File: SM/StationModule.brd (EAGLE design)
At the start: 62.2 x 36.8 mm, 25 parts, among them IC1 REG1117

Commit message: silkscreen
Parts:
- added D2: PMLL4150, diode:SOD80C
- added R5: 10k, rcl:R0805
- added R6: 33k, rcl:R0805
- added STOP: (no value), pinhead+:1X02
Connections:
- new net ADC: D2.A, R5.2, R6.1, U1.ADC
- new net STOP: R6.2, STOP.2
- net +3V3: now also STOP.1
- net GND: now also D2.C, R5.1; no longer U1.ADC
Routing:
- net ADC: track 0.00 -> 40.4 mm, vias 0 -> 2
- net +3V3: track 97.6 -> 119.7 mm
- net RESET: track 43.9 -> 54.1 mm
- net STOP: track 0.00 -> 2.86 mm
- net GND: track 226.1 -> 228.3 mm, vias 27 -> 22

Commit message: Schematic annotation
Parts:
- moved D2 2.00 mm to (27.5, 50.2), turned to 135 degrees
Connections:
- net ADC: no longer D2.A
- net GND: now also D2.A; no longer D2.C
- net STOP: now also D2.C
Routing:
- net STOP: track 2.86 -> 8.36 mm
- net ADC: track 40.4 -> 37.3 mm
- net GPIO2: track 55.8 -> 56.6 mm
- net GND: track 228.3 -> 228.6 mm, vias 22 -> 23
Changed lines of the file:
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@@
 <layer number="23" name="tOrigins" color="15" fill="1" visible="yes" active="yes"/>
 <layer number="24" name="bOrigins" color="15" fill="1" visible="yes" active="yes"/>
-<layer number="25" name="tNames" color="7" fill="1" visible="yes" active="yes"/>
-<layer number="26" name="bNames" color="7" fill="1" visible="no" active="yes"/>
+<layer number="25" name="tNames" color="7" fill="1" visible="no" active="yes"/>
+<layer number="26" name="bNames" color="7" fill="1" visible="yes" active="yes"/>
 <layer number="27" name="tValues" color="7" fill="1" visible="yes" active="yes"/>
 <layer number="28" name="bValues" color="7" fill="1" visible="no" active="yes"/>
@@
 <wire x1="81.28" y1="81.28" x2="19.05" y2="81.28" width="0" layer="20"/>
 <wire x1="19.05" y1="81.28" x2="19.05" y2="44.45" width="0" layer="20"/>
-<text x="31.75" y="34.29" size="0.762" layer="21">Portland State University
+<text x="34.29" y="38.1" size="0.762" layer="21">Portland State University
 T.Gilbert - 2107</text>
 <text x="75.184" y="71.628" size="1.27" layer="25">5V</text>
@@
 <attribute name="VALUE" x="37.465" y="49.53" size="1.27" layer="27" rot="R180"/>
 </element>
-<element name="D2" library="diode" package="SOD80C" value="PMLL4150" x="29.464" y="50.292" smashed="yes">
-<attribute name="NAME" x="27.94" y="51.435" size="1.016" layer="25"/>
+<element name="D2" library="diode" package="SOD80C" value="PMLL4150" x="27.4628125" y="50.217603125" smashed="yes" rot="R135">
+<attribute name="NAME" x="27.732221875" y="48.33175" size="1.016" layer="25" rot="R135"/>
 </element>
 </elements>
@@
 <wire x1="36.068" y1="51.054" x2="37.592" y2="49.53" width="0.6096" layer="1"/>
 <wire x1="37.592" y1="49.53" x2="43.18" y2="49.53" width="0.6096" layer="1"/>
-<contactref element="D2" pad="C"/>
-<wire x1="27.764" y1="50.292" x2="27.764" y2="51.894" width="0.6096" layer="1"/>
-<wire x1="27.764" y1="51.894" x2="27.94" y2="52.07" width="0.6096" layer="1"/>
-<wire x1="27.94" y1="52.07" x2="33.97" y2="52.07" width="0.6096" layer="1"/>
-<wire x1="33.97" y1="52.07" x2="34.29" y2="51.75" width="0.6096" layer="1"/>
 <wire x1="34.29" y1="51.75" x2="34.29" y2="53.34" width="0.6096" layer="1"/>
 <wire x1="34.29" y1="53.34" x2="36.068" y2="53.34" width="0.6096" layer="1"/>
+<contactref element="D2" pad="A"/>
+<wire x1="26.260728125" y1="51.419684375" x2="26.8804125" y2="50.8" width="0.4064" layer="1"/>
+<wire x1="26.8804125" y1="50.8" x2="31.75" y2="50.8" width="0.4064" layer="1"/>
+<wire x1="31.75" y1="50.8" x2="32.7" y2="51.75" width="0.4064" layer="1"/>
+<wire x1="32.7" y1="51.75" x2="34.29" y2="51.75" width="0.4064" layer="1"/>
+<via x="52.07" y="76.962" extent="1-16" drill="0.6"/>
 </signal>
 <signal name="GPIO1">
@@
 <via x="73.025" y="57.785" extent="1-16" drill="0.6" shape="square"/>
 <wire x1="73.025" y1="57.785" x2="71.18" y2="57.785" width="0.6096" layer="1"/>
-<wire x1="47.244" y1="70.866" x2="35.052" y2="70.866" width="0.6096" layer="16"/>
+<wire x1="54.102" y1="70.866" x2="35.052" y2="70.866" width="0.6096" layer="16"/>
 <via x="35.052" y="70.866" extent="1-16" drill="0.6" shape="square"/>
 <wire x1="35.052" y1="70.866" x2="34.925" y2="70.739" width="0.6096" layer="1"/>
 <wire x1="34.925" y1="70.739" x2="34.925" y2="68.26" width="0.6096" layer="1"/>
-<wire x1="47.244" y1="70.866" x2="48.26" y2="69.85" width="0.6096" layer="16"/>
-<wire x1="48.26" y1="69.85" x2="48.26" y2="62.738" width="0.6096" layer="16"/>
-<wire x1="48.26" y1="62.738" x2="48.768" y2="62.23" width="0.6096" layer="16"/>
 <wire x1="64.77" y1="62.23" x2="55.88" y2="62.23" width="0.6096" layer="16"/>
-<wire x1="54.61" y1="62.23" x2="48.768" y2="62.23" width="0.6096" layer="16"/>
 <wire x1="60.17" y1="61.84" x2="59.78" y2="62.23" width="0.6096" layer="1"/>
 <wire x1="59.78" y1="62.23" x2="55.88" y2="62.23" width="0.6096" layer="1"/>
 <via x="55.88" y="62.23" extent="1-16" drill="0.6" shape="square"/>
-<wire x1="55.88" y1="62.23" x2="54.61" y2="62.23" width="0.6096" layer="16"/>
+<wire x1="54.102" y1="70.866" x2="54.356" y2="70.612" width="0.6096" layer="16"/>
+<wire x1="54.356" y1="70.612" x2="54.356" y2="62.23" width="0.6096" layer="16"/>
+<wire x1="54.356" y1="62.23" x2="55.88" y2="62.23" width="0.6096" layer="16"/>
 </signal>
 <signal name="GPIO0">
@@
 <contactref element="R6" pad="2"/>
 <wire x1="35.88" y1="46.99" x2="33.02" y2="46.99" width="0.6096" layer="1"/>
+<contactref element="D2" pad="C"/>
+<wire x1="28.66489375" y1="49.01551875" x2="28.671375" y2="49.022" width="0.4064" layer="1"/>
+<wire x1="28.671375" y1="49.022" x2="31.496" y2="49.022" width="0.4064" layer="1"/>
+<wire x1="31.496" y1="49.022" x2="33.02" y2="47.498" width="0.4064" layer="1"/>
+<wire x1="33.02" y1="47.498" x2="33.02" y2="46.99" width="0.4064" layer="1"/>
 </signal>
 <signal name="ADC">
@@
 <contactref element="R5" pad="2"/>
 <contactref element="U1" pad="ADC"/>
-<contactref element="D2" pad="A"/>
 <wire x1="43.77" y1="69.84" x2="45.73" y2="69.84" width="0.6096" layer="1"/>
 <wire x1="45.73" y1="69.84" x2="46.482" y2="69.088" width="0.6096" layer="1"/>
 <via x="46.482" y="69.088" extent="1-16" drill="0.6" shape="square"/>
-<wire x1="46.482" y1="69.088" x2="46.482" y2="61.722" width="0.6096" layer="16"/>
-<wire x1="46.482" y1="61.722" x2="41.91" y2="57.15" width="0.6096" layer="16"/>
-<wire x1="41.91" y1="57.15" x2="41.91" y2="48.768" width="0.6096" layer="16"/>
+<wire x1="41.91" y1="58.42" x2="41.91" y2="48.768" width="0.6096" layer="16"/>
 <wire x1="41.91" y1="48.768" x2="41.148" y2="48.006" width="0.6096" layer="16"/>
 <via x="41.148" y="48.006" extent="1-16" drill="0.6" shape="square"/>
@@
 <wire x1="39.37" y1="46.99" x2="40.132" y2="46.99" width="0.6096" layer="1"/>
 <wire x1="40.132" y1="46.99" x2="41.148" y2="48.006" width="0.6096" layer="1"/>
-<wire x1="31.164" y1="50.292" x2="32.258" y2="50.292" width="0.6096" layer="1"/>
-<wire x1="32.258" y1="50.292" x2="33.02" y2="49.53" width="0.6096" layer="1"/>
-<wire x1="33.02" y1="49.53" x2="33.97" y2="49.53" width="0.6096" layer="1"/>
 <wire x1="33.97" y1="49.53" x2="34.29" y2="49.85" width="0.6096" layer="1"/>
 <wire x1="34.29" y1="49.85" x2="35.748" y2="49.85" width="0.6096" layer="1"/>
@@
 <wire x1="39.116" y1="48.006" x2="39.116" y2="47.244" width="0.6096" layer="1"/>
 <wire x1="39.116" y1="47.244" x2="39.37" y2="46.99" width="0.6096" layer="1"/>
-</signal>
-<signal name="N$1">
-<via x="52.07" y="76.962" extent="1-16" drill="0.6"/>
+<wire x1="46.482" y1="69.088" x2="45.72" y2="68.326" width="0.6096" layer="16"/>
+<wire x1="45.72" y1="68.326" x2="45.72" y2="62.23" width="0.6096" layer="16"/>
+<wire x1="45.72" y1="62.23" x2="41.91" y2="58.42" width="0.6096" layer="16"/>
 </signal>
 </signals>
+<errors>
+</errors>
 </board>
 </drawing>

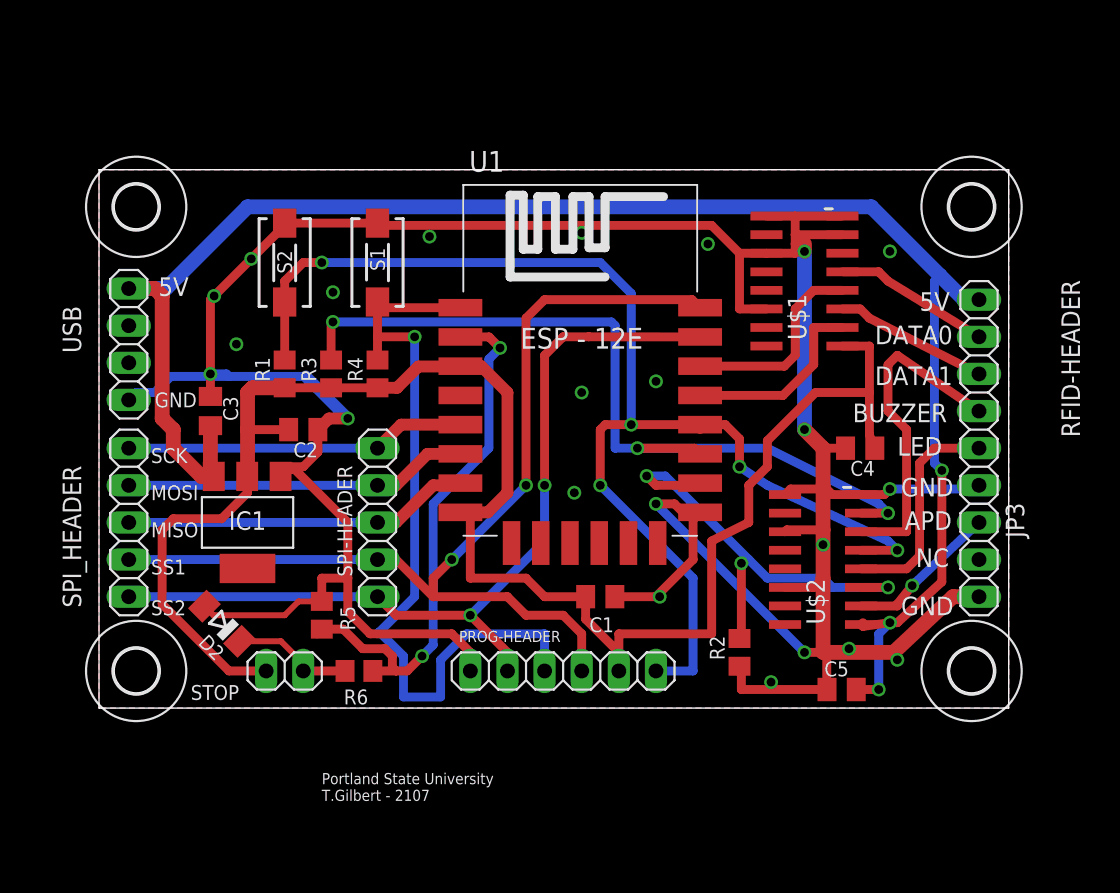
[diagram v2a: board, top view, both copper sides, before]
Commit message: SM v1.1
with fixes
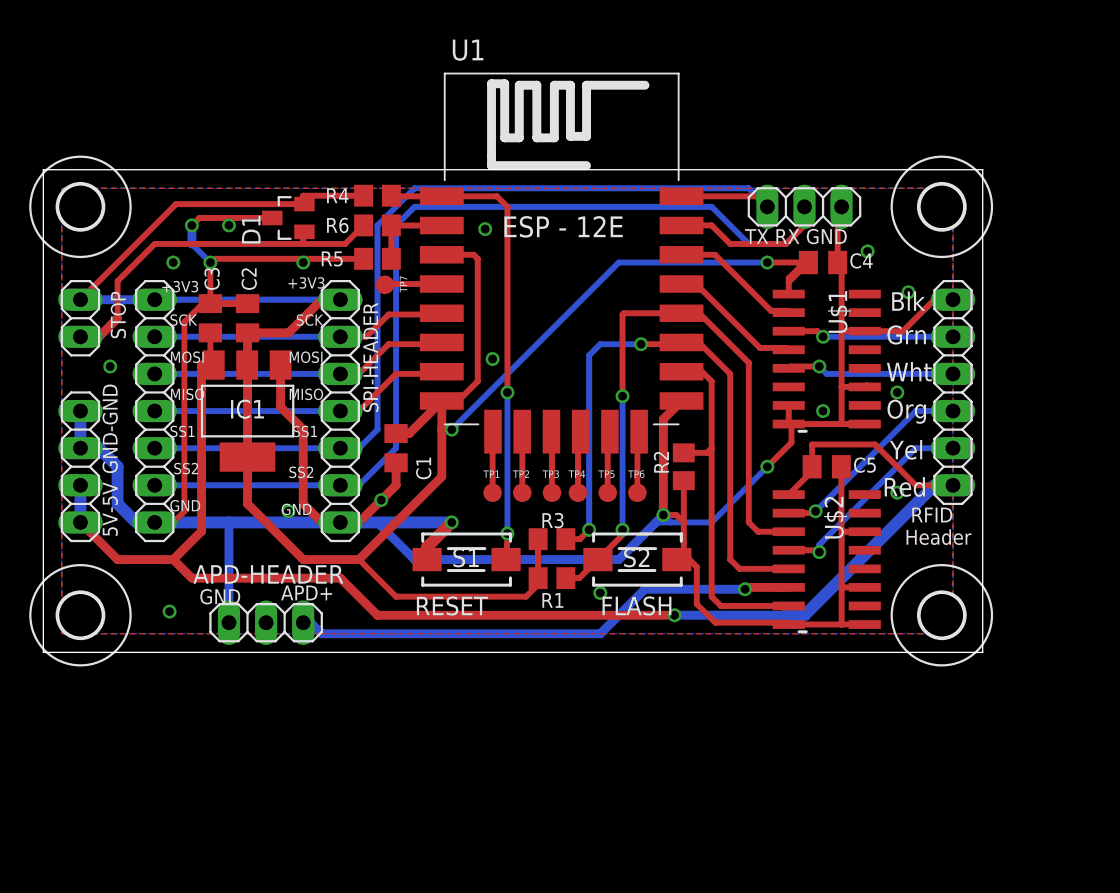
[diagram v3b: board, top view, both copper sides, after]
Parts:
- removed D2: PMLL4150, diode:SOD80C
- removed PROG-HEADER: PROG-HEADER, pinhead+:1X06
- removed SPI_HEADER: SPI-HEADER, pinhead+:1X05
- added D1: MMBZ5V6ALT1G, diode:SOT23
- added JP1: (no value), pinhead+:1X03
- added JP4: (no value), pinhead+:1X07
- added TP1, TP2, TP3, TP4, TP5, TP6, TP7: TPB1,27, testpad:B1,27
- S1: value DTSM-3 -> RESET
- S2: value DTSM-3 -> BOOT-LOADER
- SPI-HEADER: value SPI_HEADER -> (none); device pinhead+:1X05 -> pinhead+:1X07
- USB: value USB-HEADER -> 5V-Power
- moved JP3 49.0 mm to (30.5, 50.3), turned to 180 degrees
- moved S2 31.5 mm to (55.9, 54.6), turned to 0 degrees
- moved R6 30.5 mm to (38.1, 77.5)
- moved STOP 27.9 mm to (17.8, 71.1), turned to 270 degrees
- moved R5 24.7 mm to (38.1, 75.2), turned to 0 degrees
- moved R1 23.0 mm to (50.0, 53.3), turned to 180 degrees
- moved S1 21.2 mm to (44.2, 54.6), turned to 0 degrees
- moved R3 18.9 mm to (50.0, 56.0), turned to 180 degrees
- moved C1 17.3 mm to (39.4, 62.2), turned to 270 degrees
- moved C5 15.3 mm to (68.8, 61.0), turned to 0 degrees
- moved R2 13.3 mm to (59.1, 61.0)
- moved C4 13.0 mm to (68.6, 74.9), turned to 0 degrees
- moved R4 12.2 mm to (38.1, 79.5), turned to 180 degrees
- moved USB 9.01 mm to (17.8, 61.0), turned to 90 degrees
- moved C2 8.52 mm to (29.2, 71.1), turned to 270 degrees
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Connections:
- removed net D+: USB.2
- removed net D-: USB.3
- new net N$1: U$2.10
- new net N$10: TP2.TP, U1.MISO
- new net N$11: TP3.TP, U1.GPIO9
- new net N$12: TP4.TP, U1.GPIO10
- new net N$13: TP5.TP, U1.MOSI
- new net N$15: TP6.TP, U1.SCLK
- new net N$2: U$2.12
- new net N$3: U$2.15
- new net N$4: U$1.6
- new net N$5: U$1.10
- new net N$6: U$1.12
- new net N$7: U$1.15
- new net N$8: TP7.TP, U1.GPIO16
- new net N$9: TP1.TP, U1.CS0
- net +3V3: now also D1.2, IC1.4, JP4.7, SPI-HEADER.1; no longer PROG-HEADER.2
- net +5V: now also RFID-HEADER.6, USB.2; no longer RFID-HEADER.1
- net APD_EN: now also U$2.6; no longer U$2.2
- net BUZZER: now also RFID-HEADER.5, U$2.4; no longer RFID-HEADER.4, U$2.6
- net GND: now also D1.3, JP1.3, JP4.1, RFID-HEADER.1, SPI-HEADER.7, USB.3; no longer D2.A, PROG-HEADER.6, RFID-HEADER.6
- net GPIO0: now also U$2.3; no longer PROG-HEADER.1, U$2.5
- net GPIO1: now also JP1.1, JP4.3, SPI-HEADER.5; no longer PROG-HEADER.3, SPI-HEADER.4, SPI_HEADER.4
- net GPIO12: now also JP4.5, SPI-HEADER.3; no longer SPI-HEADER.2, SPI_HEADER.2
- net GPIO13: now also JP4.4, SPI-HEADER.4; no longer SPI-HEADER.3, SPI_HEADER.3
- net GPIO14: now also JP4.6, SPI-HEADER.2; no longer SPI-HEADER.1, SPI_HEADER.1
- net GPIO15: now also U$2.7; no longer U$2.3
- net GPIO2: now also U$2.5; no longer U$2.7
- net GPIO3: now also JP1.2, JP4.2, SPI-HEADER.6; no longer PROG-HEADER.5, SPI-HEADER.5, SPI_HEADER.5
- net GPIO4: now also U$1.4; no longer U$1.2
- net GPIO5: now also U$1.2; no longer U$1.4
- net GREEN_LED: now also RFID-HEADER.4, U$2.2; no longer RFID-HEADER.5, U$2.4
- net RESET: no longer PROG-HEADER.4
- net RFID-DATA0: now also U$1.3; no longer U$1.5
- net RFID-DATA1: now also U$1.5; no longer U$1.3
- net STOP: now also D1.1; no longer D2.C
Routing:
- net GPIO0: track 88.4 -> 44.2 mm, vias 5 -> 2
- net +3V3: track 119.7 -> 153.5 mm, vias 0 -> 2
- net ADC: track 37.3 -> 5.74 mm, vias 2 -> 0
- net APD_EN: track 10.5 -> 34.8 mm
- net RESET: track 54.1 -> 32.4 mm, vias 1 -> 2
- net +5V: track 118.1 -> 100.7 mm, vias 3 -> 1
- net STOP: track 8.36 -> 24.9 mm
- net GPIO3: track 59.8 -> 74.9 mm, vias 2 -> 0
- net GPIO2: track 56.6 -> 42.0 mm, vias 3 -> 2
- net BUZZER: track 22.7 -> 14.5 mm, vias 0 -> 1
- net GPIO15: track 31.4 -> 24.7 mm, vias 3 -> 0
- net GPIO1: track 70.0 -> 64.2 mm, vias 2 -> 0
- net GND: track 228.6 -> 223.0 mm, vias 23 -> 20
- net GPIO5: track 13.9 -> 8.97 mm
- net N$12: track 0.00 -> 4.36 mm
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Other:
- board size 62.2 x 36.8 mm -> 64.3 x 33 mm
- board text added: "+3V3"
- board text added: "5V-5V"
- board text added: "APD+"
- board text added: "Blk"
- board text added: "FLASH"
- board text added: "GND-GND"
- board text added: "Grn"
- board text added: "Org"
- board text added: "Portland State University Lab for Interconned Devices T.Gilbert - May 2107 v1.1"
- board text added: "RESET"
- board text added: "RFID Header"
- board text added: "Red"
- board text added: "TX RX GND"
- board text added: "Wht"
- board text added: "Yel"
- board text removed: "5V"
- board text removed: "APD"
- board text removed: "BUZZER"
- board text removed: "DATA0"
- board text removed: "DATA1"
- board text removed: "LED"
- board text removed: "NC"
- board text removed: "Portland State University T.Gilbert - 2107"
